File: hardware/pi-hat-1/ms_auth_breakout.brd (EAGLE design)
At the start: 65.5 x 57.8 mm, 41 parts, among them IC1 ULN2003AD, IC3 CPC1017, IC4 CPC1017, J11 BUCK_MODULEHORIZONTAL, J9 POWER_JACKPTH_LOCK, Q1 DMN3023L, Q2 DMN3023L, Q3 DMN3023L, Q4 DMN3023L, Q5 DMN3023L, Q6 DMN3023L

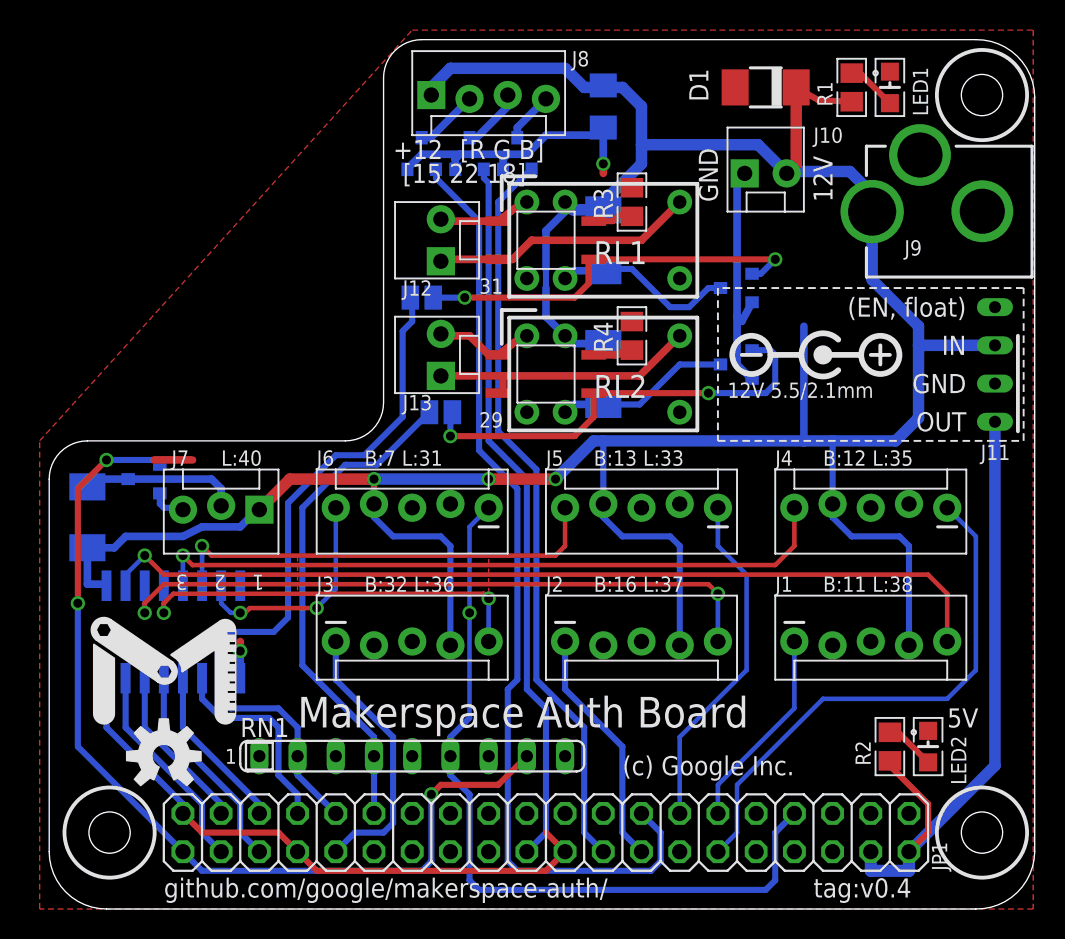
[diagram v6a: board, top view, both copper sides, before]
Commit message: Authboard change for v1.0
- Remove SOP-4 optos (most test boards we assembled with relays)
- Remove J6 (most test boards for laser need 3 outputs)
- Swap SIP resistor for 4x discrete (easier to mass-produce without it)
- Improve silkscreen around polarity and buck module
- Add MPN/MFN to parts on board.  (Should this go in schematic?)
- Change J5 to support a 3-position switch, intended for marking
  ready/needs-maintenance/down
- Leave some room for an OSH Cert number :)
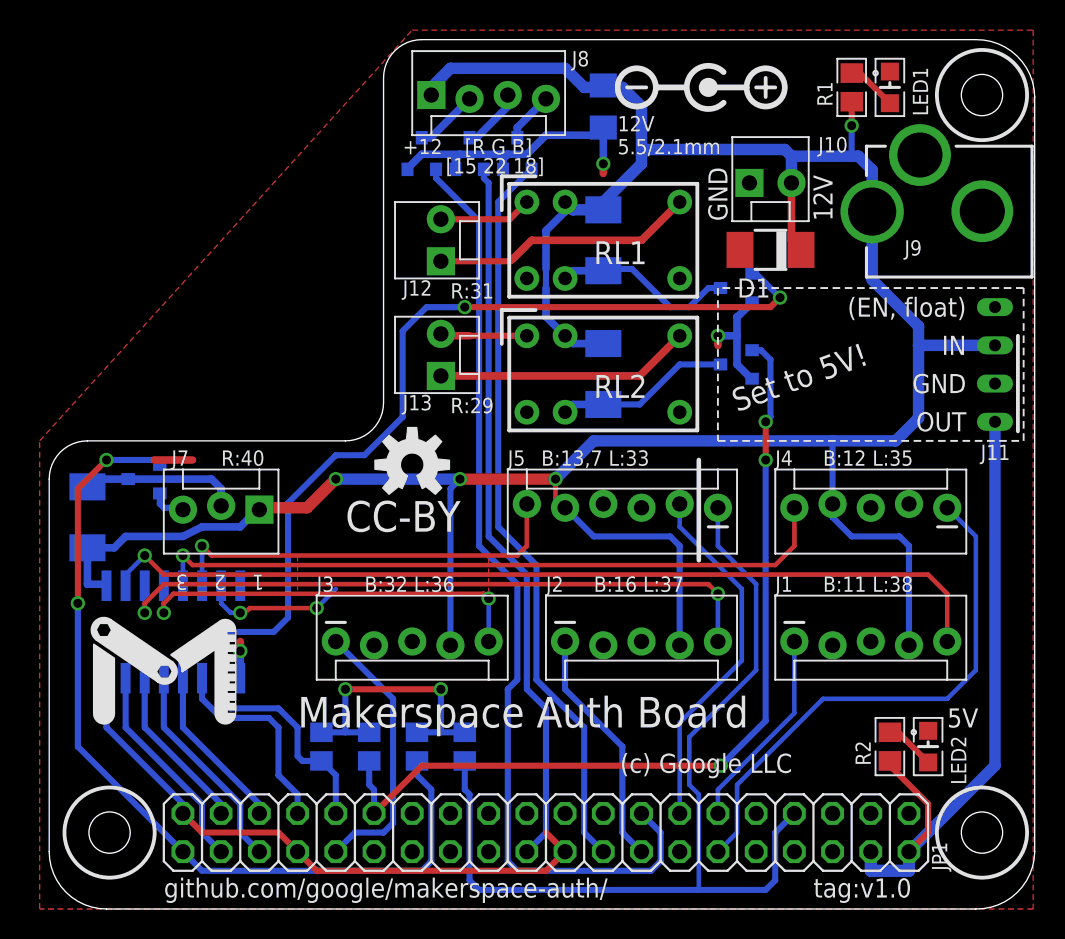
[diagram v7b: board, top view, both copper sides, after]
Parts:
- removed IC3, IC4: CPC1017, cpc1017:SOP-4
- removed J6: (no value), SparkFun-Connectors:MOLEX-1X5_LOCK
- removed RN1: (no value), resistor-sil:SIL9
- removed SJ1, SJ2: (no value), jumper:SJ
- added R5, R6: 10k, Tim-Pretty:R0805
- J5: device SparkFun-Connectors:MOLEX-1X5_LOCK -> SparkFun-Connectors:MOLEX-1X6_LOCK
- R2: value 330 -> 560
- R3, R4: value 1k -> 10k
- moved R3 41.7 mm to (19.4, 10.8), flipped to the bottom
- moved R4 32.4 mm to (22.5, 10.8), flipped to the bottom
- moved LOGO1 25.4 mm to (25.4, 29.5)
- moved D1 10.8 mm to (49.2, 43.8)
- moved J10 0.71 mm to (47.9, 48.3)
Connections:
- removed net N$13: IC4.2, R4.2
- removed net N$8: IC3.2, R3.2
- removed net RELAY_1: IC3.1, Q5.1, SJ1.1
- removed net RELAY_2: IC4.1, Q6.1, SJ2.1
- net !L5: now also J5.6; no longer J5.5
- net !L6: no longer J6.5
- net +12V: now also J5.5; no longer J5.4, J6.4
- net B5_LOGIC: now also J5.2; no longer J5.1
- net B6_LOGIC: now also J5.1, R5.2; no longer J6.1, RN1.6
- net GND: now also J5.4, R5.1, R6.1; no longer J5.3, J6.3, RN1.1, RN1.3, RN1.5, RN1.7
- net HC_LOGIC: now also R6.2; no longer RN1.8
- net L6_LOGIC: now also Q5.1, R3.2; no longer RN1.2, SJ1.2
- net L7_LOGIC: now also Q6.1, R4.2; no longer RN1.4, SJ2.2
- net N$10: no longer IC3.4
- net N$12: no longer IC4.4
- net N$6: no longer IC3.3
- net N$9: no longer IC4.3
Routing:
- net RELAY_2: track 29.2 -> 0.00 mm, vias 2 -> 0
- net L6_LOGIC: track 47.4 -> 74.1 mm, vias 0 -> 2
- net RELAY_1: track 26.6 -> 0.00 mm, vias 2 -> 0
- net L7_LOGIC: track 33.4 -> 57.8 mm, vias 0 -> 3
- net GND: track 83.5 -> 94.0 mm, vias 2 -> 5
- net +12V: track 208.1 -> 197.6 mm, vias 3 -> 4
- net B6_LOGIC: track 52.2 -> 62.4 mm, vias 1 -> 0
- net !L6: track 15.1 -> 9.71 mm
- net HC_LOGIC: track 62.5 -> 57.8 mm, vias 3 -> 2
- net N$8: track 2.72 -> 0.00 mm
- net N$13: track 2.59 -> 0.00 mm
- net !L5: track 29.8 -> 27.6 mm
- net N$12: track 18.4 -> 17.0 mm
- net B5_LOGIC: track 23.0 -> 24.2 mm
- net N$9: track 6.73 -> 6.02 mm
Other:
- board text added: "(c) Google LLC"
- board text added: "B:13,7 L:33"
- board text added: "CC-BY"
- board text added: "R:29"
- board text added: "R:31"
- board text added: "R:40"
- board text added: "Set to 5V!"
- board text added: "tag:v1.0"
- board text removed: "(c) Google Inc."
- board text removed: "29"
- board text removed: "31"
- board text removed: "B:13 L:33"
- board text removed: "B:7 L:31"
- board text removed: "L:40"
- board text removed: "tag:v0.4"

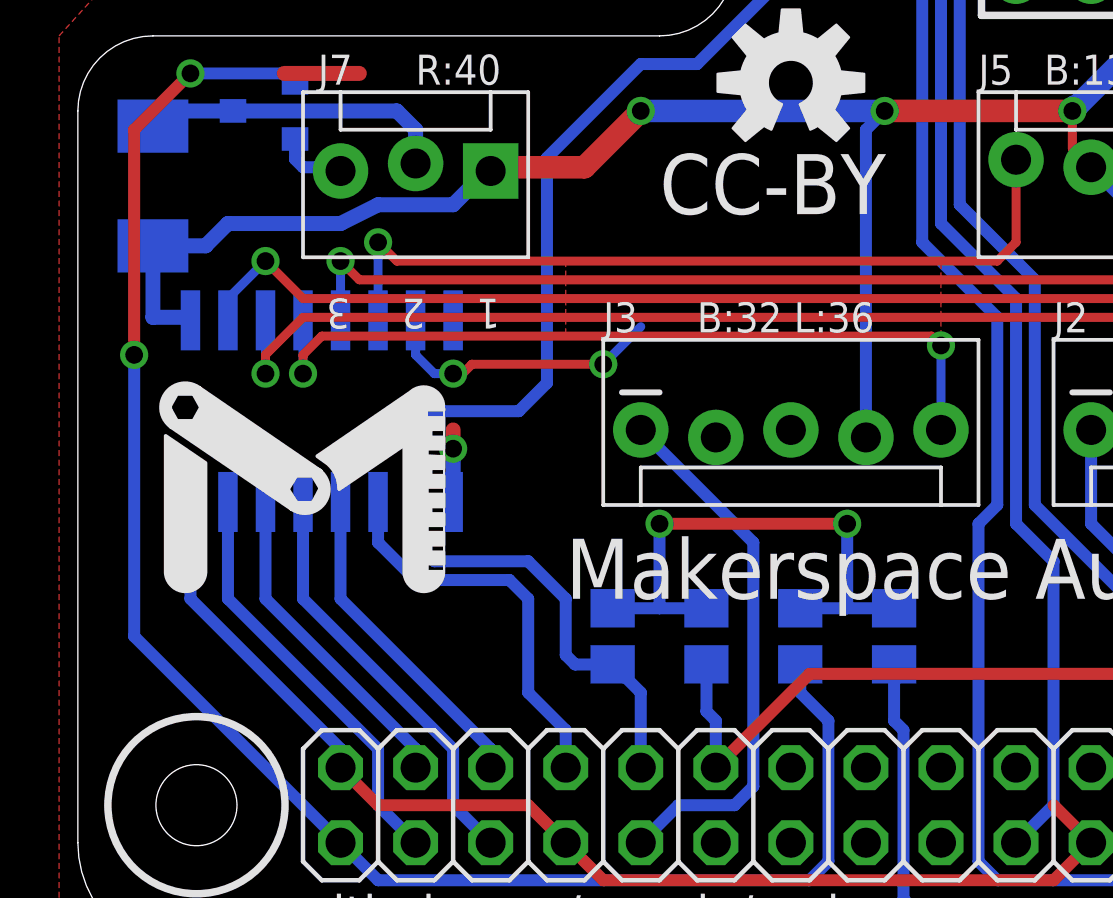
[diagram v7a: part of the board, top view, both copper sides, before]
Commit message: Add relay MPN, OSH Certification mark
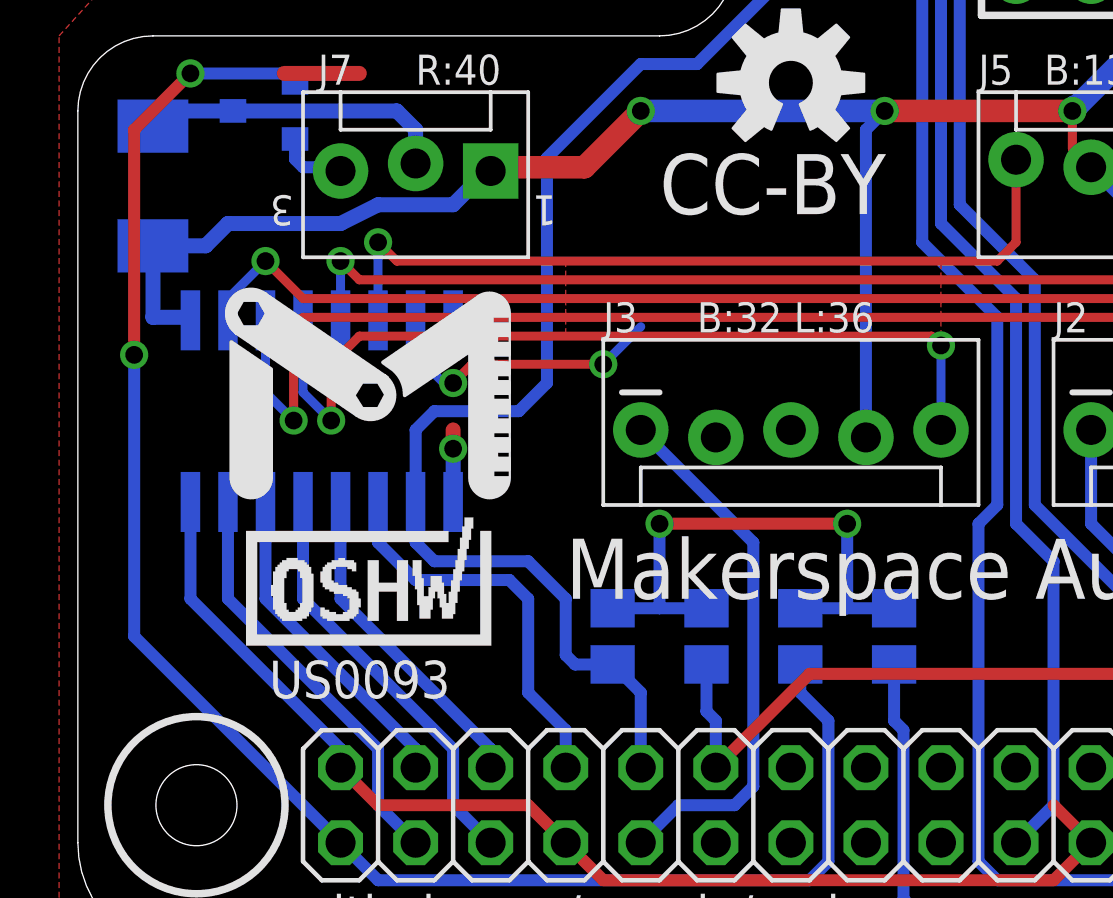
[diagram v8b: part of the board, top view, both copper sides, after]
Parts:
- added U$2: US0093, OSHWA:CERT-SMALL-SILK
- moved U$1 3.88 mm to (6.03, 15.2)
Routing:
- net !L2: track 44.5 -> 47.7 mm
- net !L3: track 27.3 -> 29.7 mm
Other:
- board text removed: "2"
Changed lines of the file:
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@@
 <text x="22.225" y="21.082" size="1.016" layer="21" ratio="20">B:32 L:36</text>
 <text x="52.705" y="21.082" size="1.016" layer="21" ratio="20">B:11 L:38</text>
-<text x="13.0175" y="22.225" size="1.016" layer="21" ratio="15" rot="SR180">2</text>
-<text x="10.4775" y="22.225" size="1.016" layer="21" ratio="15" rot="SR180">3</text>
-<text x="15.5575" y="22.225" size="1.016" layer="21" ratio="15" rot="SR180">1</text>
+<text x="8.5725" y="25.7175" size="1.016" layer="21" ratio="15" rot="SR180">3</text>
+<text x="17.4625" y="25.7175" size="1.016" layer="21" ratio="15" rot="SR180">1</text>
 <wire x1="43.18" y1="60.96" x2="43.18" y2="43.815" width="0.254" layer="51"/>
 <wire x1="43.18" y1="43.815" x2="22.225" y2="43.815" width="0.254" layer="51"/>
@@
 <attribute name="MPN" value="EMK316BBJ476ML-T" x="38.1" y="53.34" size="1.778" layer="28" rot="MR270" display="off"/>
 </element>
-<element name="U$1" library="ms-logo" package="MS_LOGO_VECTOR" value="MS_LOGO" x="3.81" y="12.065"/>
+<element name="U$1" library="ms-logo" package="MS_LOGO_VECTOR" value="MS_LOGO" x="6.0325" y="15.24"/>
 <element name="J11" library="buck-module" package="BUCK_HORIZONTAL" value="BUCK_MODULEHORIZONTAL" x="64.135" y="34.925" rot="R180"/>
 <element name="Q1" library="SparkFun-DiscreteSemi" package="SOT23-3" value="DMN3023L" x="26.035" y="50.165" smashed="yes" rot="MR0">
@@
 <element name="RL1" library="hfd23" package="HFD23" value="HFD23_SPDT" x="38.1" y="44.45" smashed="yes">
 <attribute name="NAME" x="37.465" y="42.8625" size="1.524" layer="25" font="vector"/>
-<attribute name="MPN" value="HFD23-12" x="38.1" y="44.45" size="1.778" layer="27" display="off"/>
+<attribute name="MPN" value="HFD23/012-1ZS" x="38.1" y="44.45" size="1.778" layer="27" display="off"/>
+<attribute name="MFN" value="HF" x="38.1" y="44.45" size="1.778" layer="27" display="off"/>
 </element>
 <element name="RL2" library="hfd23" package="HFD23" value="HFD23_SPDT" x="38.1" y="35.56" smashed="yes">
 <attribute name="NAME" x="37.465" y="33.9725" size="1.524" layer="25" font="vector"/>
-<attribute name="MPN" value="HFD23-12" x="38.1" y="35.56" size="1.778" layer="27" display="off"/>
+<attribute name="MPN" value="HFD23/012-1ZS" x="38.1" y="35.56" size="1.778" layer="27" display="off"/>
+<attribute name="MFN" value="HF" x="38.1" y="35.56" size="1.778" layer="27" display="off"/>
 </element>
 <element name="J13" library="SparkFun-Connectors" package="MOLEX-1X2_LOCK" value="" x="27.305" y="35.56" smashed="yes" rot="R90">
@@
 <attribute name="MPN" value="22-23-2061" x="45.72" y="26.67" size="1.778" layer="27" rot="R180" display="off"/>
 </element>
+<element name="U$2" library="OSHWA" package="CERT-SMALL-SILK" value="US0093" x="11.1125" y="10.4775"/>
 </elements>
 <signals>
@@
 <wire x1="45.72" y1="17.78" x2="45.72" y2="20.955" width="0.3048" layer="16"/>
 <via x="45.72" y="20.955" extent="1-16" drill="0.6"/>
-<wire x1="8.89" y1="21.59" x2="7.62" y2="20.32" width="0.3048" layer="1"/>
-<wire x1="7.62" y1="20.32" x2="7.62" y2="19.685" width="0.3048" layer="1"/>
-<via x="7.62" y="19.685" extent="1-16" drill="0.6"/>
-<wire x1="7.62" y1="19.685" x2="7.62" y2="21.4884" width="0.3048" layer="16"/>
+<via x="8.5725" y="18.0975" extent="1-16" drill="0.6"/>
 <wire x1="8.89" y1="21.59" x2="45.085" y2="21.59" width="0.3048" layer="1"/>
 <wire x1="45.085" y1="21.59" x2="45.72" y2="20.955" width="0.3048" layer="1"/>
+<wire x1="7.62" y1="21.4884" x2="7.62" y2="19.05" width="0.3048" layer="16"/>
+<wire x1="7.62" y1="19.05" x2="8.5725" y2="18.0975" width="0.3048" layer="16"/>
+<wire x1="8.5725" y1="18.0975" x2="8.5725" y2="21.2725" width="0.3048" layer="1"/>
+<wire x1="8.5725" y1="21.2725" x2="8.89" y2="21.59" width="0.3048" layer="1"/>
 </signal>
 <signal name="!L3">
@@
 <wire x1="30.48" y1="17.78" x2="30.48" y2="20.6375" width="0.3048" layer="16"/>
 <via x="30.48" y="20.6375" extent="1-16" drill="0.6"/>
-<via x="8.89" y="19.685" extent="1-16" drill="0.6"/>
-<wire x1="8.89" y1="19.685" x2="8.89" y2="21.4884" width="0.3048" layer="16"/>
-<wire x1="9.525" y1="20.955" x2="8.89" y2="20.32" width="0.3048" layer="1"/>
-<wire x1="8.89" y1="20.32" x2="8.89" y2="19.685" width="0.3048" layer="1"/>
-<wire x1="9.525" y1="20.955" x2="30.1625" y2="20.955" width="0.3048" layer="1"/>
+<via x="9.8425" y="18.0975" extent="1-16" drill="0.6"/>
+<wire x1="10.795" y1="20.955" x2="30.1625" y2="20.955" width="0.3048" layer="1"/>
 <wire x1="30.1625" y1="20.955" x2="30.48" y2="20.6375" width="0.3048" layer="1"/>
+<wire x1="10.795" y1="20.955" x2="9.8425" y2="20.0025" width="0.3048" layer="1"/>
+<wire x1="9.8425" y1="20.0025" x2="9.8425" y2="18.0975" width="0.3048" layer="1"/>
+<wire x1="8.89" y1="21.4884" x2="8.89" y2="19.05" width="0.3048" layer="16"/>
+<wire x1="8.89" y1="19.05" x2="9.8425" y2="18.0975" width="0.3048" layer="16"/>
 </signal>
 <signal name="!L4">
@@
 <signal name="!L6">
 <contactref element="IC1" pad="15"/>
-<wire x1="13.335" y1="19.685" x2="12.7" y2="20.32" width="0.3048" layer="16"/>
 <wire x1="12.7" y1="20.32" x2="12.7" y2="21.4884" width="0.3048" layer="16"/>
 <wire x1="20.32" y1="21.2725" x2="19.05" y2="20.0025" width="0.3048" layer="16"/>
 <via x="19.05" y="20.0025" extent="1-16" drill="0.6"/>
 <wire x1="19.05" y1="20.0025" x2="14.605" y2="20.0025" width="0.3048" layer="1"/>
-<wire x1="14.605" y1="20.0025" x2="14.2875" y2="19.685" width="0.3048" layer="1"/>
-<wire x1="14.2875" y1="19.685" x2="13.97" y2="19.685" width="0.3048" layer="1"/>
-<via x="13.97" y="19.685" extent="1-16" drill="0.6"/>
-<wire x1="13.97" y1="19.685" x2="13.335" y2="19.685" width="0.3048" layer="16"/>
+<wire x1="14.605" y1="20.0025" x2="13.97" y2="19.3675" width="0.3048" layer="1"/>
+<via x="13.97" y="19.3675" extent="1-16" drill="0.6"/>
+<wire x1="13.97" y1="19.3675" x2="13.6525" y2="19.3675" width="0.3048" layer="16"/>
+<wire x1="13.6525" y1="19.3675" x2="12.7" y2="20.32" width="0.3048" layer="16"/>
 </signal>
 <signal name="N$1">
